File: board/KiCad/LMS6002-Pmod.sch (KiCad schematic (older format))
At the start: 0 parts

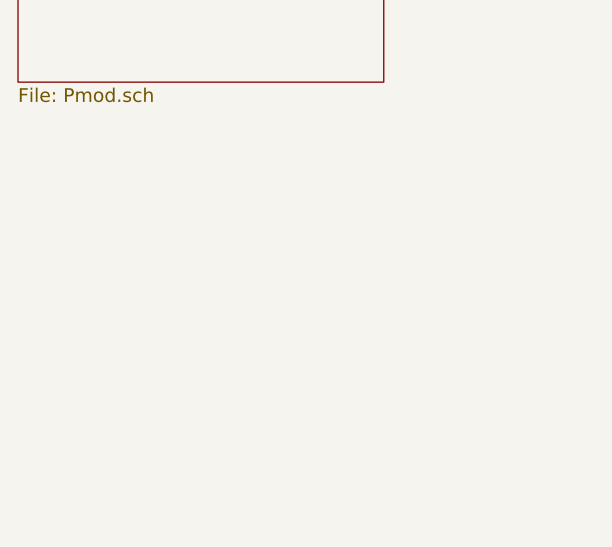
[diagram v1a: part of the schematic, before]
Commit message: 1.2V power supply
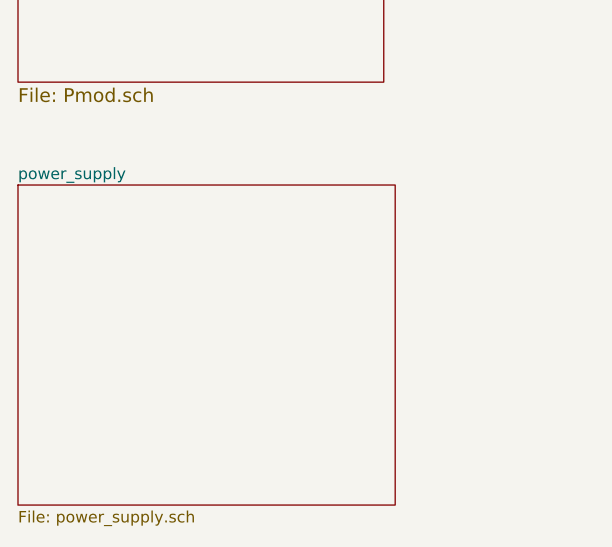
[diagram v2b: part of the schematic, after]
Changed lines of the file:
@@
 EESchema Schematic File Version 2
+LIBS:LMS6002-Pmod-rescue
 LIBS:power
 LIBS:device
@@
 $Descr A4 11693 8268
 encoding utf-8
-Sheet 1 4
+Sheet 1 5
 Title ""
 Date ""
@@
 F1 "myriadrf.sch" 60
 $EndSheet
+$Sheet
+S 1900 3050 1650 1400
+U 56A67CE4
+F0 "power_supply" 50
+F1 "power_supply.sch" 50
+$EndSheet
 $EndSCHEMATC

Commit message: SPI & Osci
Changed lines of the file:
@@
 $Descr A4 11693 8268
 encoding utf-8
-Sheet 1 5
+Sheet 1 6
 Title ""
 Date ""
@@
 F1 "power_supply.sch" 50
 $EndSheet
+$Sheet
+S 5050 3050 1550 1400
+U 56BBAE88
+F0 "SPI_Interface" 60
+F1 "SPI_Interface.sch" 60
+$EndSheet
 $EndSCHEMATC

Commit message: Add OSHW Logo
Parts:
- added T1: OSHW_Logo, Symbols:Symbol_OSHW-Logo_SilkScreen, symbol OSHW_Logo
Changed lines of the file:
@@
 F1 "SPI_Interface.sch" 60
 $EndSheet
+$Comp
+L OSHW_Logo T1
+U 1 1 56C98252
+P 9500 3700
+F 0 "T1" H 9603 3753 60  0000 L CNN
+F 1 "OSHW_Logo" H 9603 3647 60  0000 L CNN
+F 2 "Symbols:Symbol_OSHW-Logo_SilkScreen" H 9500 3700 60  0001 C CNN
+F 3 "" H 9500 3700 60  0000 C CNN
+	1    9500 3700
+	1    0    0    -1
+$EndComp
 $EndSCHEMATC
